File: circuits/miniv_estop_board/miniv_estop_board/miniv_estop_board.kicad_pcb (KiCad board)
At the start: 2 copper layers, 100 x 130 mm, 39 parts, among them J1 Conn_Main_DCDC, J2 Conn_neopixel_01, J3 Conn_neopixel_02, J4 Conn_neopixel_03, J5 Conn_neopixel_04, J6 EStop_button, J7 EStop_signal0, J8 EStop_signal1, Q1 2SJ555-E, Q2 NPN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

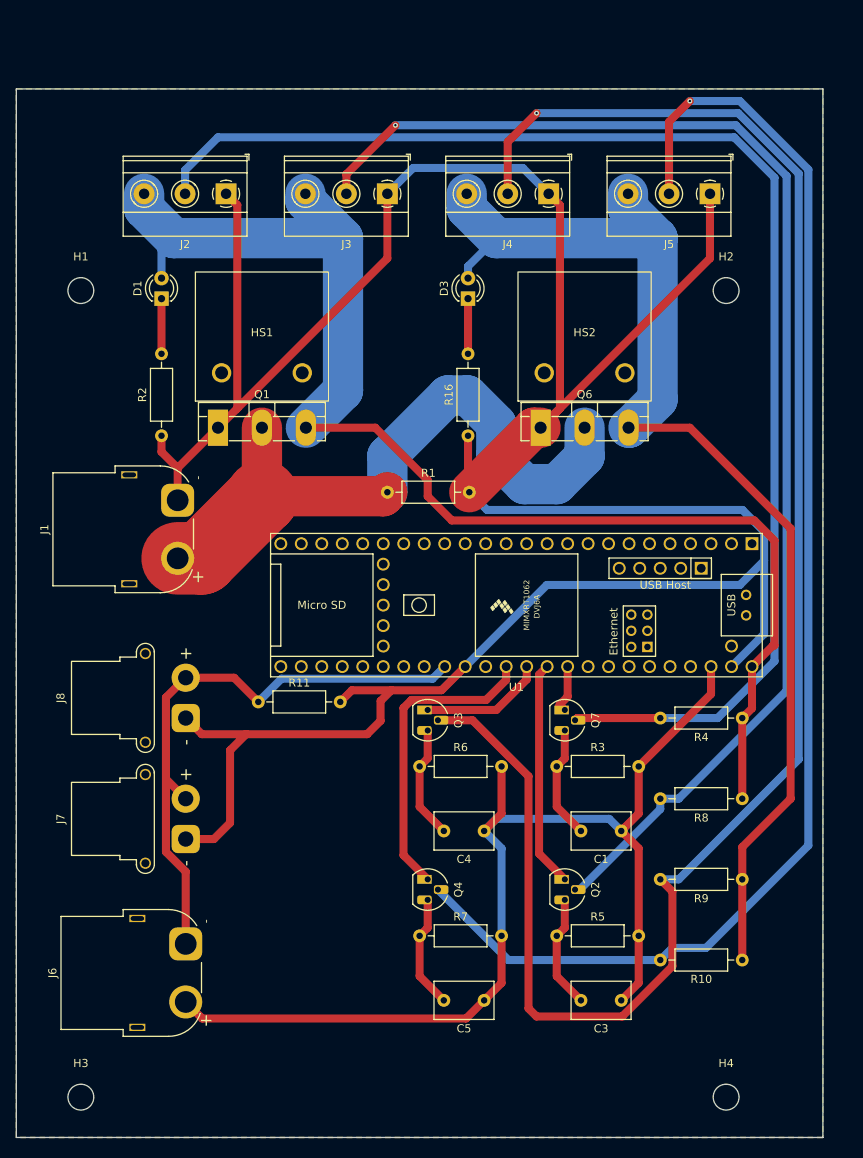
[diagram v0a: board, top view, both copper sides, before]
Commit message: Feature/add capaciter regester for neopixel (#383)
* add capaciter

Signed-off-by: Masaya Kataoka <ms.kataoka@gmail.com>

* update bom

Signed-off-by: Masaya Kataoka <ms.kataoka@gmail.com>

* update pcb

Signed-off-by: Masaya Kataoka <ms.kataoka@gmail.com>

---------

Signed-off-by: Masaya Kataoka <ms.kataoka@gmail.com>
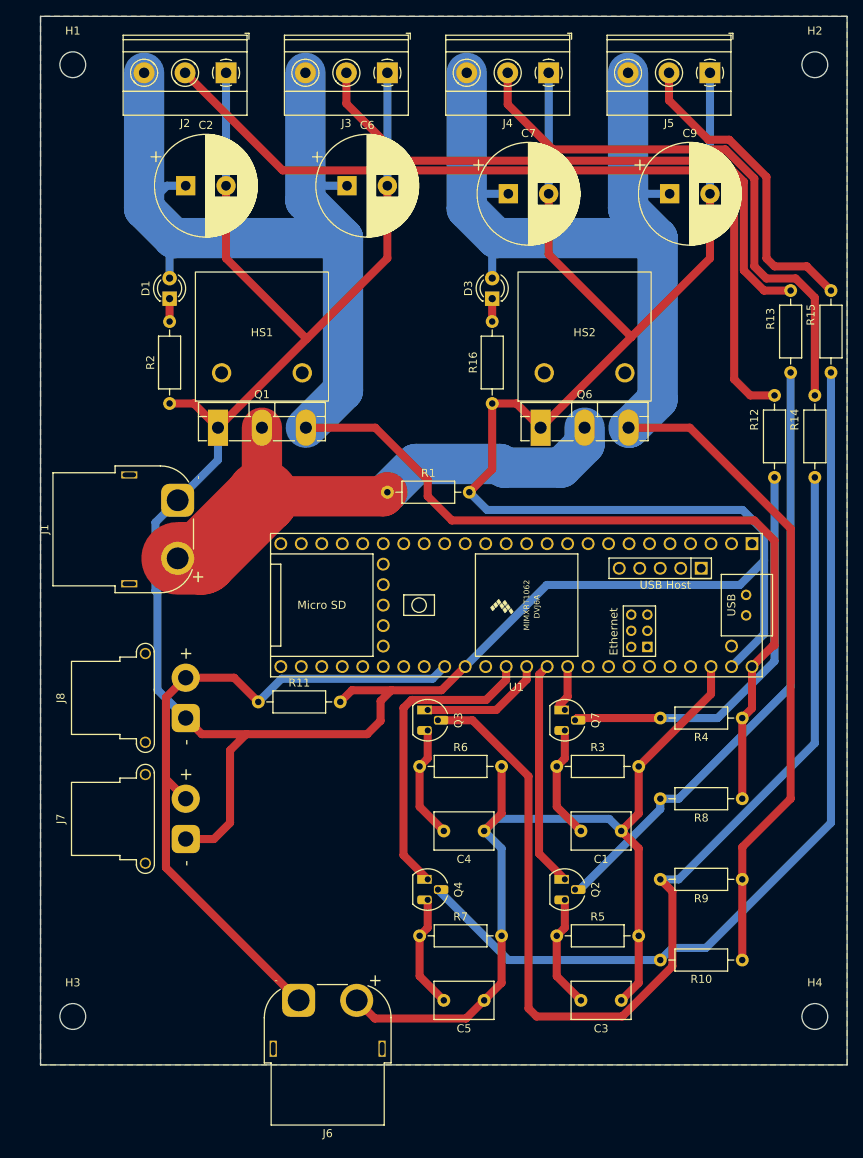
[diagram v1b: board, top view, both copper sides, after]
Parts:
- added C2: 1000μ, Capacitor_THT:CP_Radial_D12.5mm_P5.00mm, F.Cu at (110.0, 34.0)
- added C6: 1000μ, Capacitor_THT:CP_Radial_D12.5mm_P5.00mm, F.Cu at (130.0, 34.0)
- added C7: 1000μ, Capacitor_THT:CP_Radial_D12.5mm_P5.00mm, F.Cu at (150.0, 35.0)
- added C9: 1000μ, Capacitor_THT:CP_Radial_D12.5mm_P5.00mm, F.Cu at (170.0, 35.0)
- added R12: 470, Resistor_THT:R_Axial_DIN0207_L6.3mm_D2.5mm_P10.16mm_Horizontal, F.Cu at (183.0, 60.0)
- added R13: 470, Resistor_THT:R_Axial_DIN0207_L6.3mm_D2.5mm_P10.16mm_Horizontal, F.Cu at (185.0, 47.0)
- added R14: 470, Resistor_THT:R_Axial_DIN0207_L6.3mm_D2.5mm_P10.16mm_Horizontal, F.Cu at (188.0, 60.0)
- added R15: 470, Resistor_THT:R_Axial_DIN0207_L6.3mm_D2.5mm_P10.16mm_Horizontal, F.Cu at (190.0, 47.0)
- moved H2 30.1 mm to (188.0, 19.0)
- moved H1 28.0 mm to (96.0, 19.0)
- moved J6 15.7 mm to (124.0, 135.0), turned to 180 degrees
- moved J2 15.0 mm to (115.0, 20.0)
- moved J3 15.0 mm to (135.0, 20.0)
- moved J4 15.0 mm to (155.0, 20.0)
- moved J5 15.0 mm to (175.0, 20.0)
- moved H4 14.9 mm to (188.0, 137.0)
- moved H3 10.0 mm to (96.0, 137.0)
- moved R16 5.00 mm to (148.0, 61.0)
- moved R2 4.12 mm to (108.0, 61.0)
- moved D3 3.00 mm to (148.0, 48.0)
- moved D1 1.00 mm to (108.0, 48.0)
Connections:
- Q2 pad 2: Net-(J3-Pin_2) -> Net-(Q2-C)
- Q3 pad 2: Net-(J4-Pin_2) -> Net-(Q3-C)
- Q4 pad 2: Net-(J5-Pin_2) -> Net-(Q4-C)
- Q7 pad 2: Net-(J2-Pin_2) -> Net-(Q7-C)
- R10 pad 2: Net-(J5-Pin_2) -> Net-(Q4-C)
- R4 pad 2: Net-(J2-Pin_2) -> Net-(Q7-C)
- R8 pad 2: Net-(J3-Pin_2) -> Net-(Q2-C)
- R9 pad 2: Net-(J4-Pin_2) -> Net-(Q3-C)
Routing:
- net Net-(J4-Pin_2): track 218.2 -> 70.4 mm, vias 1 -> 0
- net Net-(Q3-C): track 0.00 -> 134.2 mm
- net Net-(J5-Pin_2): track 170.0 -> 39.2 mm, vias 1 -> 0
- net Net-(Q4-C): track 0.00 -> 115.2 mm
- net Net-(J3-Pin_2): track 163.1 -> 74.9 mm, vias 1 -> 0
- net Net-(Q2-C): track 0.00 -> 76.9 mm
- net Net-(J2-Pin_2): track 167.5 -> 103.7 mm
- net GND: track 355.9 -> 412.1 mm
- net Net-(Q7-C): track 0.00 -> 50.6 mm
- net Net-(D1-A): track 165.3 -> 207.1 mm
- net Net-(D3-A): track 146.8 -> 187.4 mm
- net Net-(J6-Pin_2): track 136.5 -> 115.4 mm
- net Net-(J1-Pin_2): track 81.9 -> 67.3 mm
- net Net-(J6-Pin_1): track 73.7 -> 86.5 mm
- net Net-(D3-K): track 6.84 -> 2.84 mm
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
